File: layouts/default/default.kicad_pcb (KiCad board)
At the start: 2 copper layers, 86 parts

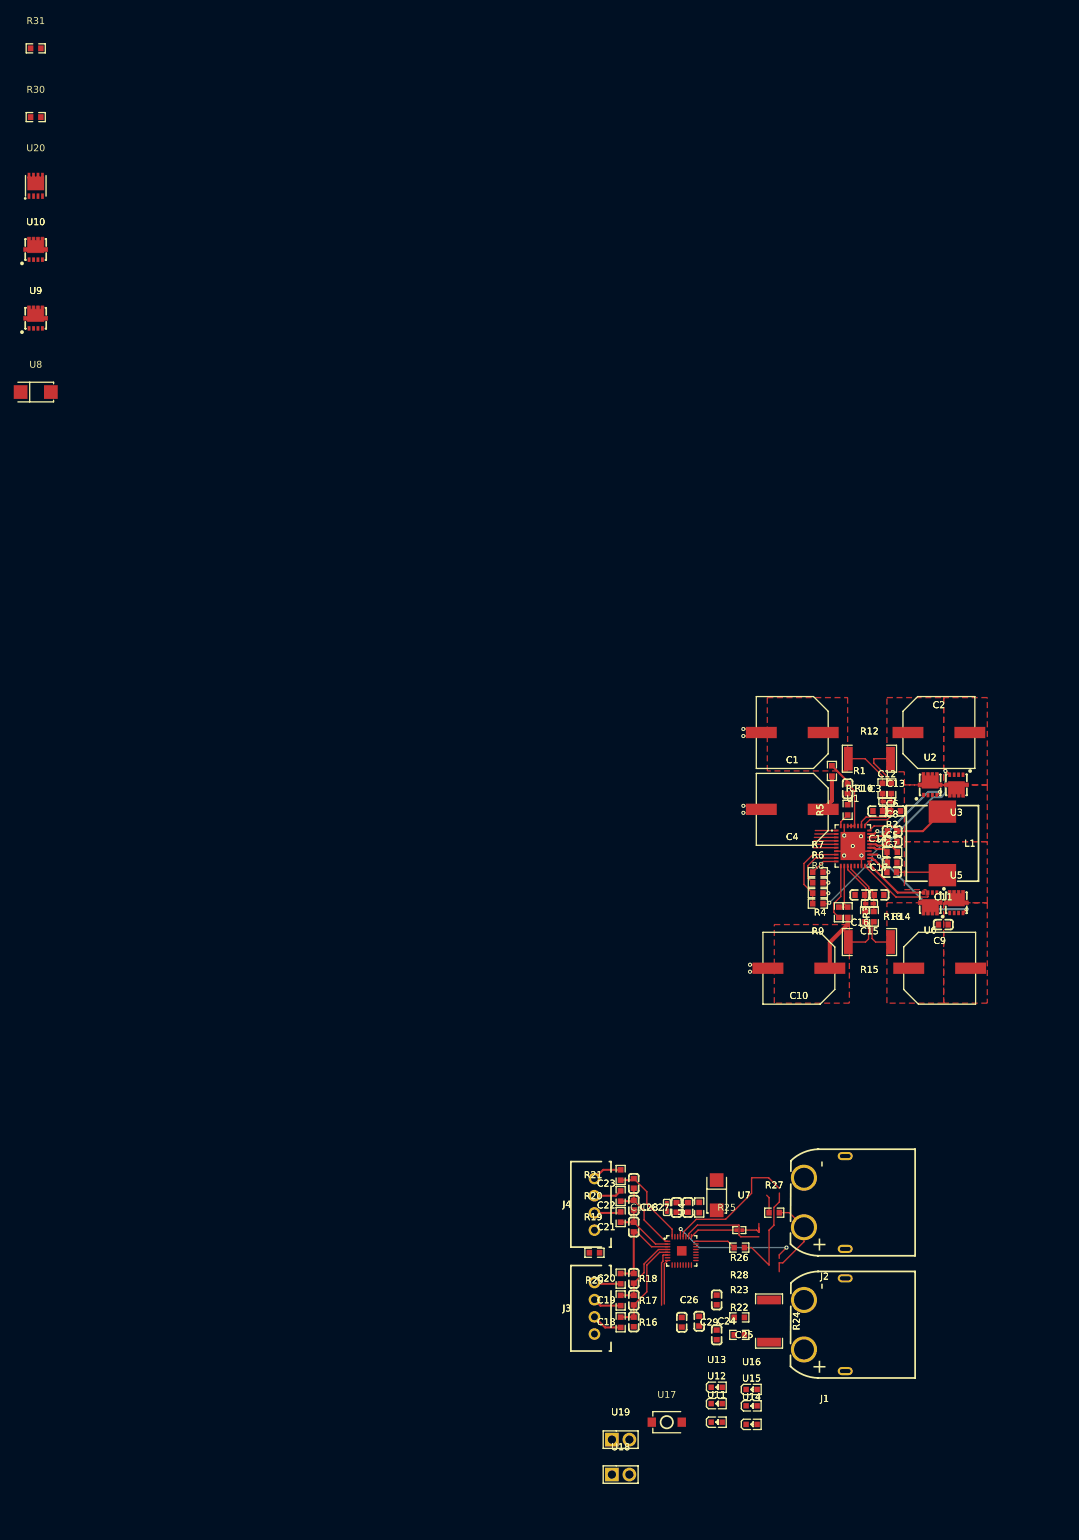
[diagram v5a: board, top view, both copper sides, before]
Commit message: Work on battery monitor
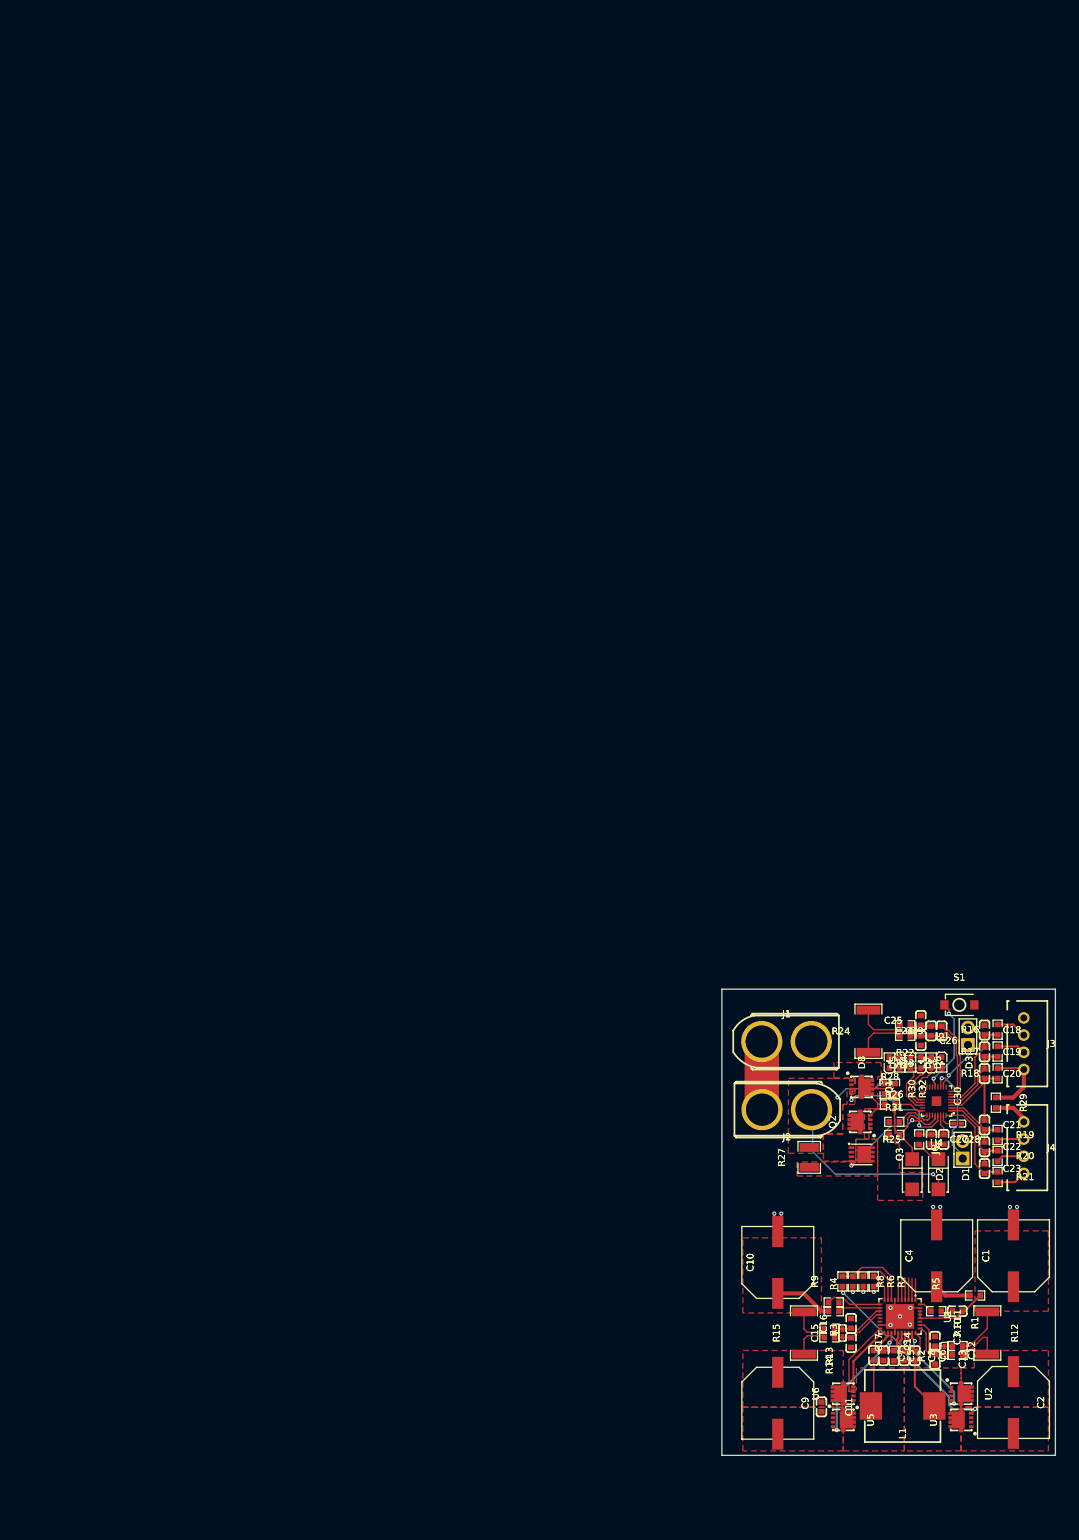
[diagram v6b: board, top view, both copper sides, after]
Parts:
- removed U10, U9: , HL_40N06D:WDFN-5_L3.3-W3.3-P0.65-BL
- removed U11, U12, U13, U14, U15, U16: , Hubei_KENTO_Elec_KT_0603R:LED0603-RD
- removed U17: , XUNPU_TS_1088_AR02016:SW-SMD_L3.9-W3.0-P4.45
- removed U18, U19: , XFCN_PZ254V_11_02P:HDR-TH_2P-P2.54-V-M
- removed U20: , XNRUSEMI_XR15P06D:DFN-8_L3.0-W3.0-P0.65-BL-4
- removed U7, U8: , MDD_Microdiode_Electronics_SS34:SMA_L4.3-W2.6-LS5.2-RD
- added D1: , MDD_Microdiode_Electronics_SS34:SMA_L4.3-W2.6-LS5.2-RD, F.Cu at (131.3, 113.8)
- added D2: , MDD_Microdiode_Electronics_SS34:SMA_L4.3-W2.6-LS5.2-RD, F.Cu at (127.5, 113.8)
- added D3: , Hubei_KENTO_Elec_KT_0603R:LED0603-RD, F.Cu at (131.8, 97.5)
- added D4: , Hubei_KENTO_Elec_KT_0603R:LED0603-RD, F.Cu at (130.3, 97.5)
- added D5: , Hubei_KENTO_Elec_KT_0603R:LED0603-RD, F.Cu at (128.8, 97.5)
- added D6: , Hubei_KENTO_Elec_KT_0603R:LED0603-RD, F.Cu at (127.2, 97.5)
- added D7: , Hubei_KENTO_Elec_KT_0603R:LED0603-RD, F.Cu at (125.7, 97.5)
- added D8: , Hubei_KENTO_Elec_KT_0603R:LED0603-RD, F.Cu at (124.2, 97.5)
- added J5: , XFCN_PZ254V_11_02P:HDR-TH_2P-P2.54-V-M, F.Cu at (135.6, 93.7)
- added J6: , XFCN_PZ254V_11_02P:HDR-TH_2P-P2.54-V-M, F.Cu at (134.9, 110.2)
- added Q1: , HL_40N06D:WDFN-5_L3.3-W3.3-P0.65-BL, F.Cu at (119.4, 101.1)
- added Q2: , HL_40N06D:WDFN-5_L3.3-W3.3-P0.65-BL, F.Cu at (120.7, 106.2)
- added Q3: , XNRUSEMI_XR15P06D:DFN-8_L3.0-W3.0-P0.65-BL-4, F.Cu at (120.2, 110.9)
- added R32: 10MΩ ±1% 100mW, YAGEO_RC0603FR_0710ML:R0603, F.Cu at (125.0, 101.4)
- added S1: , XUNPU_TS_1088_AR02016:SW-SMD_L3.9-W3.0-P4.45, F.Cu at (134.4, 89.2)
- J1, J2: footprint Changzhou_Amass_Elec_XT60PW_M:CONN-TH_XT60PW-M -> Changzhou_Amass_Elec_XT60U_M:CONN-TH_XT60U-M
- R26: value 10kΩ ±1% 62.5mW -> 10kΩ ±1% 100mW; footprint UNI_ROYAL_0402WGF1002TCE:R0402 -> UNI_ROYAL_0603WAF1002T5E:R0603
- R27: value 1kΩ ±1% 100mW -> 1kΩ ±5% 500mW; footprint UNI_ROYAL_0603WAF1001T5E:R0603 -> UNI_ROYAL_1210W2J0102T5E:R1210
- moved R31 201.5 mm to (124.9, 108.1)
- moved R30 187.7 mm to (123.5, 101.4), turned to -90 degrees
- moved C2 98.1 mm to (142.2, 147.0), turned to -90 degrees
- moved U3 93.1 mm to (135.4, 149.5), turned to 90 degrees
- moved U2 87.9 mm to (133.9, 145.7), turned to -90 degrees
- moved R12 85.3 mm to (138.4, 136.9), turned to -90 degrees
- moved R10 83.0 mm to (134.1, 140.1), turned to 0 degrees
- moved C1 82.7 mm to (142.2, 125.7), turned to 90 degrees
- moved L1 82.0 mm to (126.1, 147.5), turned to 180 degrees
- moved R11 81.9 mm to (134.1, 138.8), turned to 0 degrees
- moved C12 80.3 mm to (132.2, 139.4), turned to -90 degrees
- moved C13 79.9 mm to (130.8, 140.7), turned to -90 degrees
- moved R1 79.1 mm to (136.7, 131.4), turned to 180 degrees
- moved C3 77.6 mm to (134.1, 133.7), turned to 180 degrees
- moved C14 77.6 mm to (130.8, 138.1), turned to 90 degrees
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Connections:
- R30 pad 1: pack.r_qchg-net-0 -> vbat
- R30 pad 2: pack.r_qchg-net-1 -> CHG
- R31 pad 1: pack.r_qdsg-net-0 -> pack_p
- R31 pad 2: pack.r_qdsg-net-1 -> pack-cathode-1
- U4 pad 21: pack-cathode-1 -> pack-cathode-2
- U4 pad 22: pack-cathode-2 -> pack-cathode-3
- U4 pad 26: DSG -> pack-cathode-1
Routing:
- net (no net): track 87.6 -> 0.00 mm, vias 2 -> 0
- net vbat: track 0.00 -> 35.9 mm, vias 0 -> 3
- net CHG: track 0.00 -> 20.1 mm, vias 0 -> 3
- net pack-cathode-1: track 0.00 -> 18.9 mm
- net PCHG: track 0.00 -> 16.7 mm, vias 0 -> 2
- net pack-anode: track 0.00 -> 16.6 mm, vias 0 -> 2
- net TS2: track 0.00 -> 15.2 mm, vias 0 -> 1
- net pack-cathode-2: track 0.00 -> 13.9 mm
- net nDISP_TS4_ADCIN2_GPIO: track 0.00 -> 13.9 mm, vias 0 -> 2
- net pack-cathode-3: track 0.00 -> 12.1 mm
- net pack-D-0: track 0.00 -> 10.8 mm
- net pack-gnd-2: track 0.00 -> 9.92 mm
- net pack-SRN: track 8.03 -> 17.2 mm
- net pack-SRP: track 6.53 -> 15.5 mm
- net TS1: track 0.00 -> 7.58 mm, vias 0 -> 1
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- added copper zone on F.Cu, net pack-D-0
- added copper zone on F.Cu, net pack-D-1
- added copper zone on F.Cu, net pack_p
- added copper zone on F.Cu, net vbat
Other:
- board outline added: 48.5 x 67.8 mm

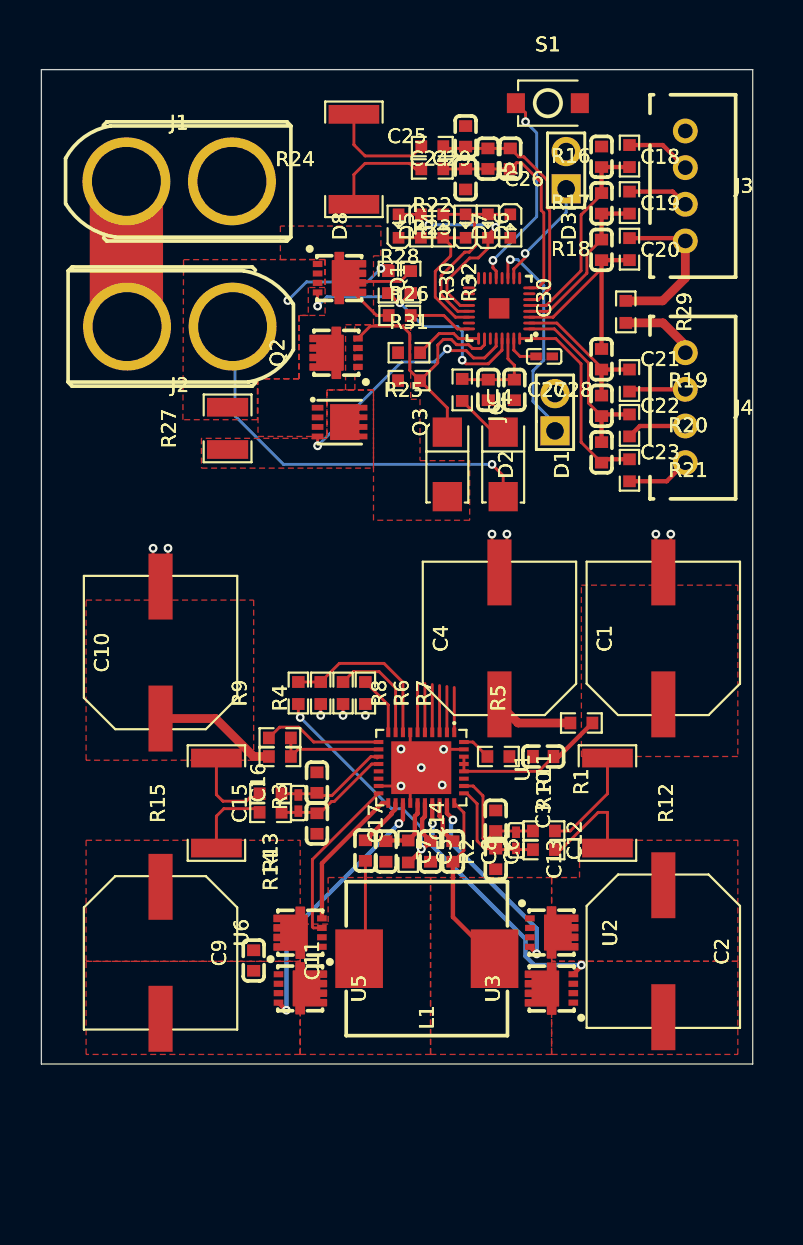
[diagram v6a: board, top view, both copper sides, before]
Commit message: join monitor and charger
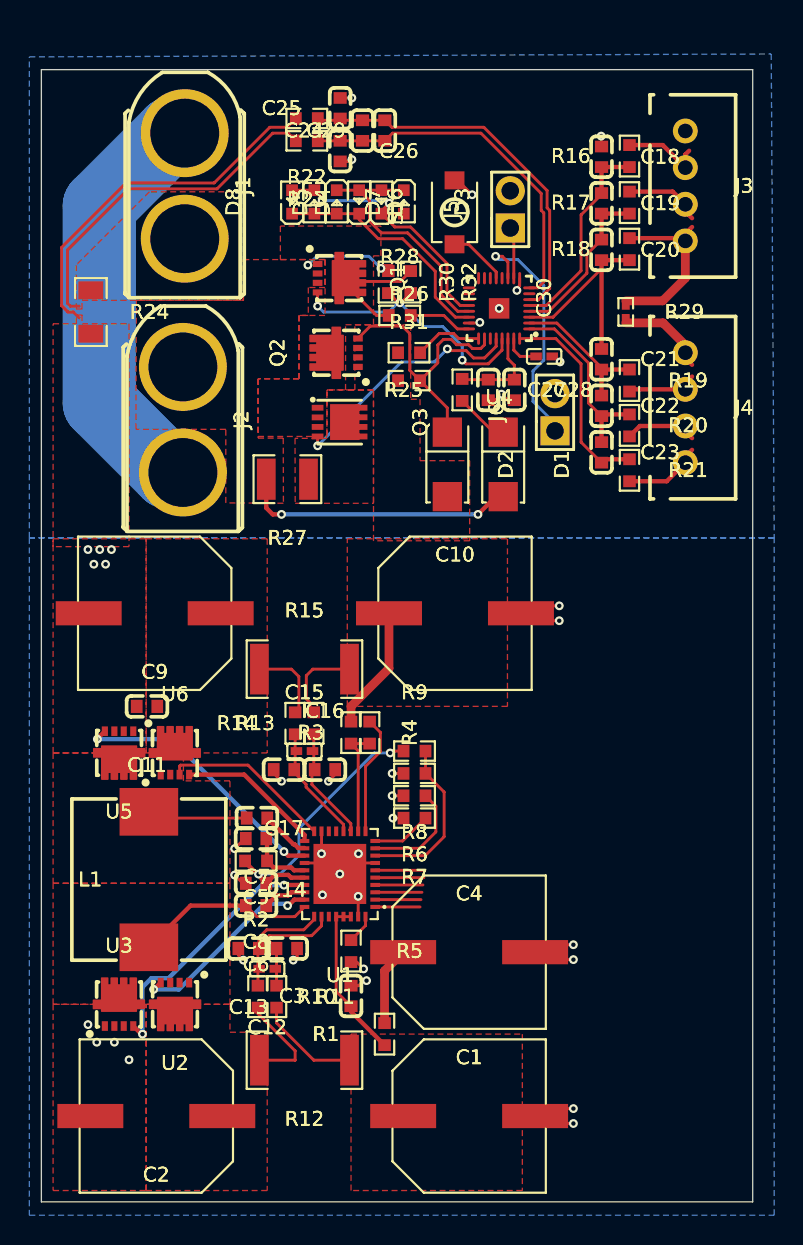
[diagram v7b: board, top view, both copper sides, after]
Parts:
- R24: value 1mΩ ±1% 3W -> 1mΩ ±1% 1W; footprint Milliohm_HoYLR2512E_3W_1mR_1:R2512 -> YAGEO_PA1206FRF470R001L:R1206
- R29: value 0Ω 100mW -> 0Ω 62.5mW; footprint UNI_ROYAL_0603WAF0000T5E:R0603 -> UNI_ROYAL_0402WGF0000TCE:R0402
- R4: footprint YAGEO_RT0603BRD07249KL:R0603 -> PANASONIC_ERA3AEB2493V:R0603
- moved C2 36.4 mm to (107.7, 158.2), turned to 180 degrees
- moved C1 35.2 mm to (129.0, 158.2), turned to 0 degrees
- moved U3 30.3 mm to (105.1, 151.4), turned to 0 degrees
- moved R12 27.1 mm to (117.8, 154.4), turned to 180 degrees
- moved U2 25.3 mm to (108.9, 149.9), turned to 180 degrees
- moved R1 25.1 mm to (123.2, 152.6), turned to 90 degrees
- moved C9 23.2 mm to (107.5, 123.9), turned to 180 degrees
- moved R10 21.9 mm to (114.6, 150.1), turned to -90 degrees
- moved C4 21.5 mm to (129.0, 147.1), turned to 0 degrees
- moved R11 21.5 mm to (115.9, 150.1), turned to -90 degrees
- moved C3 20.9 mm to (120.9, 150.0), turned to 90 degrees
- moved R24 20.7 mm to (103.2, 103.4), turned to -90 degrees
- moved U5 20.4 mm to (105.1, 132.7), turned to 180 degrees
- moved C10 20.3 mm to (128.0, 123.9), turned to 0 degrees
- moved L1 19.7 mm to (107.2, 142.1), turned to 90 degrees
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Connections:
- C1 pad 2: -gnd -> neg
- C10 pad 2: -gnd -> neg
- C11 pad 2: -gnd -> neg
- C13 pad 2: -gnd -> neg
- C14 pad 2: -gnd -> neg
- C16 pad 2: -gnd -> neg
- C17 pad 2: -gnd -> neg
- C18 pad 1: -gnd -> pack-gnd-0
- C2 pad 2: -gnd -> neg
- C25 pad 2: pack-gnd-1 -> pack-gnd-0
- C26 pad 2: pack-gnd-1 -> pack-gnd-0
- C27 pad 2: -gnd -> pack-gnd-0
- C28 pad 2: -gnd -> pack-gnd-0
- C3 pad 2: -gnd -> neg
- C30 pad 2: -gnd -> pack-gnd-0
- C4 pad 2: -gnd -> neg
- C5 pad 2: -gnd -> neg
- C8 pad 2: -gnd -> neg
- C9 pad 2: -gnd -> neg
- D2 pad 2: pack_p -> vsys
- J1 pad 1: pack-gnd-1 -> pack-gnd-0
- J3 pad 4: -gnd -> pack-gnd-0
- J4 pad 4: pack-gnd-0 -> pack-gnd-1
- J5 pad 2: -gnd -> pack-gnd-0
- J6 pad 2: -gnd -> pack-gnd-0
- Q2 pad 1: pack_p -> vsys
- Q2 pad 2: pack_p -> vsys
- Q2 pad 3: pack_p -> vsys
- R22 pad 2: pack_n -> neg
- R23 pad 2: -gnd -> pack-gnd-0
- R24 pad 1: -gnd -> pack-gnd-0
- R24 pad 2: pack_n -> neg
- R26 pad 1: pack_p -> vsys
- R29 pad 2: pack-gnd-0 -> pack-gnd-1
- R31 pad 1: pack_p -> vsys
- R5 pad 2: -gnd -> neg
- R6 pad 2: -gnd -> neg
- R7 pad 2: -gnd -> neg
- R8 pad 2: -gnd -> neg
- S1 pad 2: -gnd -> pack-gnd-0
- U1 pad 17: -gnd -> neg
- U1 pad 22: -gnd -> neg
- U1 pad 35: -gnd -> neg
- U1 pad 37: -gnd -> neg
- U1 pad 7: -gnd -> neg
- U3 pad 1: -gnd -> neg
- U3 pad 2: -gnd -> neg
- U3 pad 3: -gnd -> neg
- U4 pad 23: -gnd -> pack-gnd-0
- U4 pad 33: -gnd -> pack-gnd-0
- U4 pad 9: -gnd -> pack-gnd-0
- U5 pad 1: -gnd -> neg
- U5 pad 2: -gnd -> neg
- U5 pad 3: -gnd -> neg
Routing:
- net neg: track 0.00 -> 64.8 mm, vias 0 -> 31
- net -gnd: track 37.9 -> 0.00 mm, vias 14 -> 0
- net pack-gnd-0: track 5.20 -> 32.1 mm, vias 0 -> 9
- net pack-gnd-2: track 9.92 -> 29.0 mm
- net vbat: track 35.9 -> 25.2 mm, vias 3 -> 4
- net nDISP_TS4_ADCIN2_GPIO: track 13.9 -> 4.05 mm, vias 2 -> 0
- net pack-SRP: track 15.5 -> 24.5 mm
- net pack-SRN: track 17.2 -> 26.1 mm
- net pack_n: track 7.25 -> 0.00 mm
- net pack-gnd-1: track 0.00 -> 6.22 mm
- net pack-cathode-3: track 12.1 -> 16.3 mm
- net TS1: track 7.58 -> 3.52 mm, vias 1 -> 0
- net pack-cathode-2: track 13.9 -> 17.4 mm
- net pack-anode: track 16.6 -> 19.3 mm
- net TS2: track 15.2 -> 17.1 mm
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- added copper zone on B.Cu, net neg
- added copper zone on F.Cu, net neg
- added copper zone on B.Cu, net pack-gnd-0
- added copper zone on F.Cu, net pack-gnd-0
- removed copper zone on F.Cu, net -gnd
- removed copper zone on F.Cu, net pack_p
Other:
- board size 48.5 x 67.8 mm -> 48.5 x 77.2 mm

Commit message: Add connectors for Power in/out, and I2C
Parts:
- added J7: , JST_Sales_America_B4B_XH_A_LF__SN:CONN-TH_B4B-XH-A-LF-SN, F.Cu at (139.0, 138.8)
- added J8: , Changzhou_Amass_Elec_XT60U_M:CONN-TH_XT60U-M, F.Cu at (141.0, 125.4)
- added J9: , Changzhou_Amass_Elec_XT60U_M:CONN-TH_XT60U-M, F.Cu at (141.0, 152.0)
- turned S1 to -90 degrees
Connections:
- net neg renamed -gnd
- C1 pad 1: charger-pos-0 -> -pos
- C11 pad 1: charger-pos-3 -> charger-pos-2
- C2 pad 1: charger-pos-1 -> charger-pos-0
- C3 pad 1: charger-pos-0 -> -pos
- C4 pad 1: charger-pos-2 -> charger-pos-1
- C9 pad 1: charger-pos-3 -> charger-pos-2
- R1 pad 1: charger-pos-0 -> -pos
- R1 pad 2: charger-pos-2 -> charger-pos-1
- R10 pad 2: charger-pos-1 -> charger-pos-0
- R11 pad 2: charger-pos-0 -> -pos
- R12 pad 1: charger-pos-0 -> -pos
- R12 pad 2: charger-pos-1 -> charger-pos-0
- R14 pad 2: charger-pos-3 -> charger-pos-2
- R15 pad 1: charger-pos-3 -> charger-pos-2
- U1 pad 32: charger-pos-0 -> -pos
- U1 pad 33: charger-pos-0 -> -pos
- U1 pad 34: charger-pos-0 -> -pos
- U2 pad 5: charger-pos-1 -> charger-pos-0
- U4 pad 18: SMBD -> SDA
- U4 pad 19: SMBC -> SCL
- U6 pad 5: charger-pos-3 -> charger-pos-2
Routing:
- net SCL: track 3.06 -> 80.3 mm, vias 0 -> 1
- net SDA: track 3.13 -> 76.4 mm, vias 0 -> 1
- net -pos: track 0.00 -> 18.2 mm
- net charger-pos-0: track 18.2 -> 7.07 mm
- net -gnd: track 64.8 -> 75.7 mm, vias 31 -> 35
- net charger-pos-3: track 5.44 -> 0.00 mm
- net nDISP_TS4_ADCIN2_GPIO: track 4.05 -> 8.13 mm
- net charger-pos-1: track 7.07 -> 5.36 mm
- net CHG: track 19.5 -> 21.1 mm
- net pack-c1-0: track 5.71 -> 4.45 mm
- net pack-c3-0: track 12.3 -> 11.1 mm
- net pack-c2-0: track 5.31 -> 4.17 mm
- net pack-c1-1: track 4.93 -> 3.87 mm
- net pack-c3-1: track 5.40 -> 4.34 mm
- net pack-gnd-1: track 6.22 -> 5.20 mm
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- added copper zone on F.Cu, net -pos
- added copper zone on F.Cu, net charger-pos-2
- removed copper zone on F.Cu, net charger-pos-1
- removed copper zone on F.Cu, net charger-pos-3
